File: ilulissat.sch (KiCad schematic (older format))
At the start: 29 parts, among them J1 Conn_01x04, SW1 ~RST~, SW2 USR, U1 EFR32MG21x, U2 HDC2080, Y1 32.768Khz, Y2 38.4Mhz

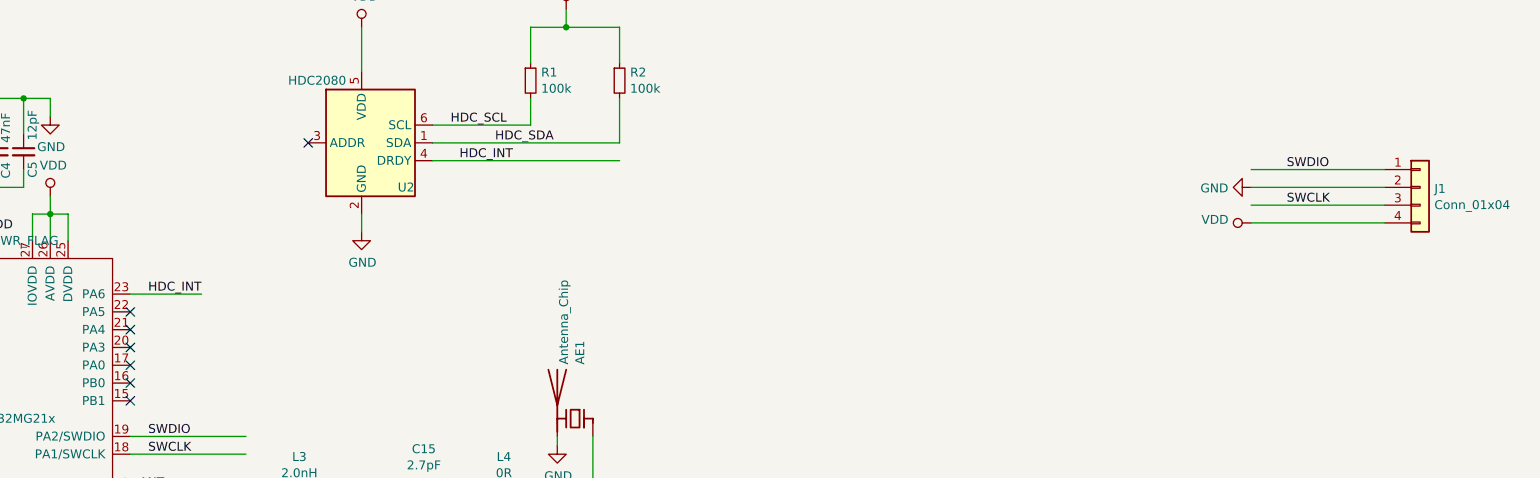
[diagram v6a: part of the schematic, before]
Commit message: Add UART
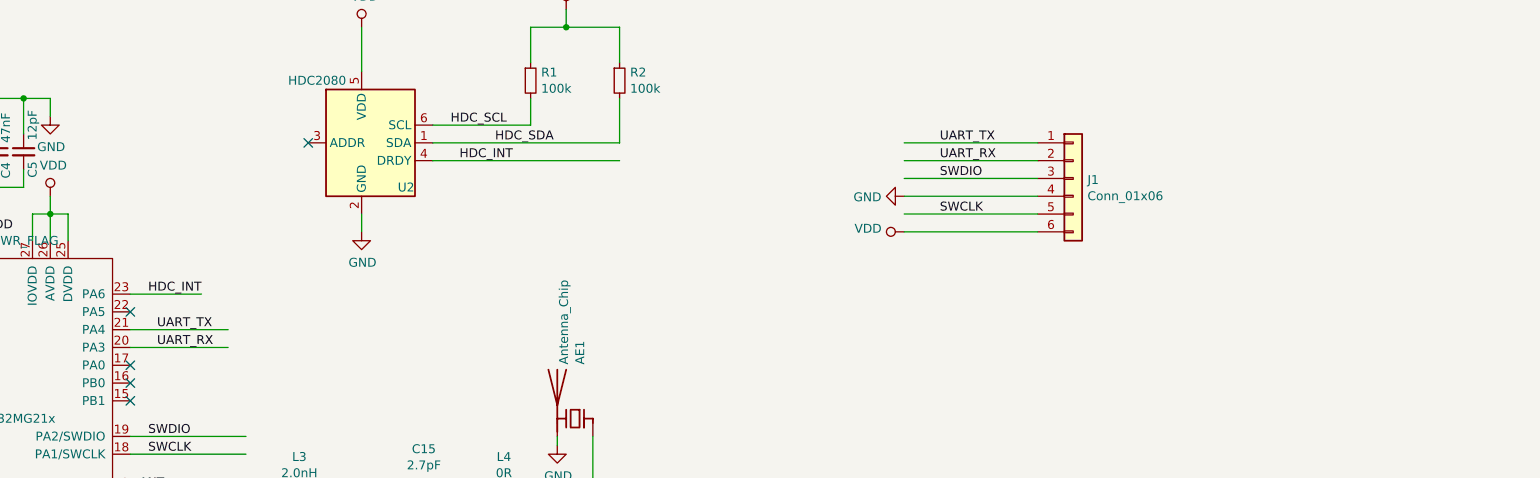
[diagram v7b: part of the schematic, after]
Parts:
- removed J1: Conn_01x04, Connector_PinHeader_1.27mm:PinHeader_1x04_P1.27mm_Vertical, symbol Connector_Generic:Conn_01x04
- added J1: Conn_01x06, Connector_PinHeader_1.27mm:PinHeader_1x06_P1.27mm_Vertical, symbol Connector_Generic:Conn_01x06
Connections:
- net labels added: UART_RX, UART_TX
- wire segments 119 -> 123
- no-connect marks 13 -> 11
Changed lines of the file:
@@
 HDC_INT
 Wire Wire Line
-	10700 2300 9950 2300
+	8750 2350 8000 2350
 $Comp
 L power:GND #PWR015
@@
 Text Label 1800 3250 0    50   ~ 0
 HDC_SCL
-NoConn ~ 3650 3100
 NoConn ~ 3650 3200
 NoConn ~ 3650 3300
@@
 Wire Wire Line
 	1000 1550 1000 1650
-Text Label 10150 2100 0    50   ~ 0
+Text Label 8200 2150 0    50   ~ 0
 SWDIO
-Text Label 10150 2300 0    50   ~ 0
+Text Label 8200 2350 0    50   ~ 0
 SWCLK
 $Comp
@@
 -
 Wire Wire Line
-	10700 2100 9950 2100
+	8750 2150 8000 2150
 Text Label 2500 2400 1    50   ~ 0
 PAVDD
@@
 NoConn ~ 2150 3350
 NoConn ~ 3650 2900
-NoConn ~ 3650 3000
-$Comp
-L Connector_Generic:Conn_01x04 J1
-U 1 1 5E470F09
-P 10900 2200
-F 0 "J1" H 10980 2192 50  0000 L CNN
-F 1 "Conn_01x04" H 10980 2101 50  0000 L CNN
-F 2 "Connector_PinHeader_1.27mm:PinHeader_1x04_P1.27mm_Vertical" H 10900 2200 50  0001 C CNN
-F 3 "~" H 10900 2200 50  0001 C CNN
-	1    10900 2200
-	1    0    0    -1
-$EndComp
 $Comp
 L power:GND #PWR019
 U 1 1 5E47862B
-P 9950 2200
-F 0 "#PWR019" H 9950 1950 50  0001 C CNN
-F 1 "GND" V 9955 2072 50  0000 R CNN
-F 2 "" H 9950 2200 50  0001 C CNN
-F 3 "" H 9950 2200 50  0001 C CNN
-	1    9950 2200
-	0    1    1    0
-$EndComp
-Wire Wire Line
-	10700 2200 9950 2200
+P 8000 2250
+F 0 "#PWR019" H 8000 2000 50  0001 C CNN
+F 1 "GND" V 8005 2122 50  0000 R CNN
+F 2 "" H 8000 2250 50  0001 C CNN
+F 3 "" H 8000 2250 50  0001 C CNN
+	1    8000 2250
+	0    1    1    0
+$EndComp
+Wire Wire Line
+	8750 2250 8000 2250
 $Comp
 L power:VDD #PWR020
 U 1 1 5E47C814
-P 9950 2400
-F 0 "#PWR020" H 9950 2250 50  0001 C CNN
-F 1 "VDD" V 9968 2527 50  0000 L CNN
-F 2 "" H 9950 2400 50  0001 C CNN
-F 3 "" H 9950 2400 50  0001 C CNN
-	1    9950 2400
+P 8000 2450
+F 0 "#PWR020" H 8000 2300 50  0001 C CNN
+F 1 "VDD" V 8018 2577 50  0000 L CNN
+F 2 "" H 8000 2450 50  0001 C CNN
+F 3 "" H 8000 2450 50  0001 C CNN
+	1    8000 2450
 	0    -1   -1   0
 $EndComp
 Wire Wire Line
-	10700 2400 9950 2400
+	8750 2450 8000 2450
 $Comp
 L Switch:SW_SPST SW2
@@
 Text Label 1700 3450 0    50   ~ 0
 ~USRBTN~
+Text Label 3800 3000 0    50   ~ 0
+UART_TX
+Text Label 3800 3100 0    50   ~ 0
+UART_RX
+Wire Wire Line
+	3650 3100 4200 3100
+Wire Wire Line
+	3650 3000 4200 3000
+$Comp
+L Connector_Generic:Conn_01x06 J1
+U 1 1 5E513834
+P 8950 2150
+F 0 "J1" H 9030 2142 50  0000 L CNN
+F 1 "Conn_01x06" H 9030 2051 50  0000 L CNN
+F 2 "Connector_PinHeader_1.27mm:PinHeader_1x06_P1.27mm_Vertical" H 8950 2150 50  0001 C CNN
+F 3 "~" H 8950 2150 50  0001 C CNN
+	1    8950 2150
+	1    0    0    -1
+$EndComp
+Text Label 8200 1950 0    50   ~ 0
+UART_TX
+Text Label 8200 2050 0    50   ~ 0
+UART_RX
+Wire Wire Line
+	8000 1950 8750 1950
+Wire Wire Line
+	8000 2050 8750 2050
 $EndSCHEMATC

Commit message: Add LED
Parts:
- added D1: RED, LED_SMD:LED_0402_1005Metric, symbol Device:LED_Small
- added R3: 360R, Resistor_SMD:R_0402_1005Metric, symbol Device:R_Small
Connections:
- net labels added: USRLED
- wire segments 123 -> 127
- no-connect marks 11 -> 10
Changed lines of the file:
@@
 	2450 1250 2450 1300
 Connection ~ 2450 1250
-NoConn ~ 2150 3350
 NoConn ~ 3650 2900
 $Comp
@@
 Wire Wire Line
 	8000 2050 8750 2050
+Wire Wire Line
+	2150 3350 1500 3350
+Text Label 1700 3350 0    50   ~ 0
+USRLED
+$Comp
+L Device:R_Small R3
+U 1 1 5E5419C9
+P 1400 3350
+F 0 "R3" V 1204 3350 50  0000 C CNN
+F 1 "360R" V 1295 3350 50  0000 C CNN
+F 2 "Resistor_SMD:R_0402_1005Metric" H 1400 3350 50  0001 C CNN
+F 3 "~" H 1400 3350 50  0001 C CNN
+	1    1400 3350
+	0    1    1    0
+$EndComp
+$Comp
+L Device:LED_Small D1
+U 1 1 5E542201
+P 1100 3350
+F 0 "D1" H 1100 3585 50  0000 C CNN
+F 1 "RED" H 1100 3494 50  0000 C CNN
+F 2 "LED_SMD:LED_0402_1005Metric" V 1100 3350 50  0001 C CNN
+F 3 "~" V 1100 3350 50  0001 C CNN
+	1    1100 3350
+	1    0    0    -1
+$EndComp
+Wire Wire Line
+	1300 3350 1200 3350
+$Comp
+L power:GND #PWR021
+U 1 1 5E546EAB
+P 950 3400
+F 0 "#PWR021" H 950 3150 50  0001 C CNN
+F 1 "GND" H 955 3227 50  0000 C CNN
+F 2 "" H 950 3400 50  0001 C CNN
+F 3 "" H 950 3400 50  0001 C CNN
+	1    950  3400
+	1    0    0    -1
+$EndComp
+Wire Wire Line
+	1000 3350 950  3350
+Wire Wire Line
+	950  3350 950  3400
 $EndSCHEMATC
